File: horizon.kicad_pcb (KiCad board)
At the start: 4 copper layers, 50 x 100 mm, 261 parts, among them IC1 A3909, J1 Micro_SD_Card_Det1, J10 Conn_01x02_Pin, J11 USB_C_Receptacle_USB2.0_16P, J12 Conn_01x04, J13 1x3 servo, J14 1x3 servo, J15 arming terminal, J16 arming terminal, J17 arming terminal, J18 arming terminal, J19 Screw_Terminal_01x02, J2 Conn_02x03_Counter_Clockwise, J20 Screw_Terminal_01x02, J21 Screw_Terminal_01x02, J22 Screw_Terminal_01x02, J23 USB_C_Receptacle_USB2.0_16P, J24 USB_C_Receptacle_USB2.0_16P, J25 Conn_Coaxial, J3 Conn_Coaxial, J4 H9161TR-ND, J5 Screw_Term, J6 1x3 servo, J7 Conn_02x03_Counter_Clockwise, J8 Conn_02x03_Counter_Clockwise, J9 1x3 servo, Q1 IRLML6402, Q10 IRLML6402, Q11 IRLML6402, Q2 DMG2301L, Q3 IRLML6402, Q4 IRLML6402, Q5 IRLML6402, Q6 IRLML6402, Q7 BSS138, Q8 IRLML6402, Q9 IRLML6402, U1 MMCU, U10 LSM6DS3, U11 BGM220SC12WGA2R, U12 PE4259, U13 LTC4412xS6, U14 TPS61092, U15 AP2112K-3.3, U2 IMU, U3 NMCU, U4 TMCU, U5 LPS22HB, U6 GPS, U7 SX1276, U8 NAND, U9 TPS82130, Y1 Crystal, Y2 32.768kHz, Y4 32MHz

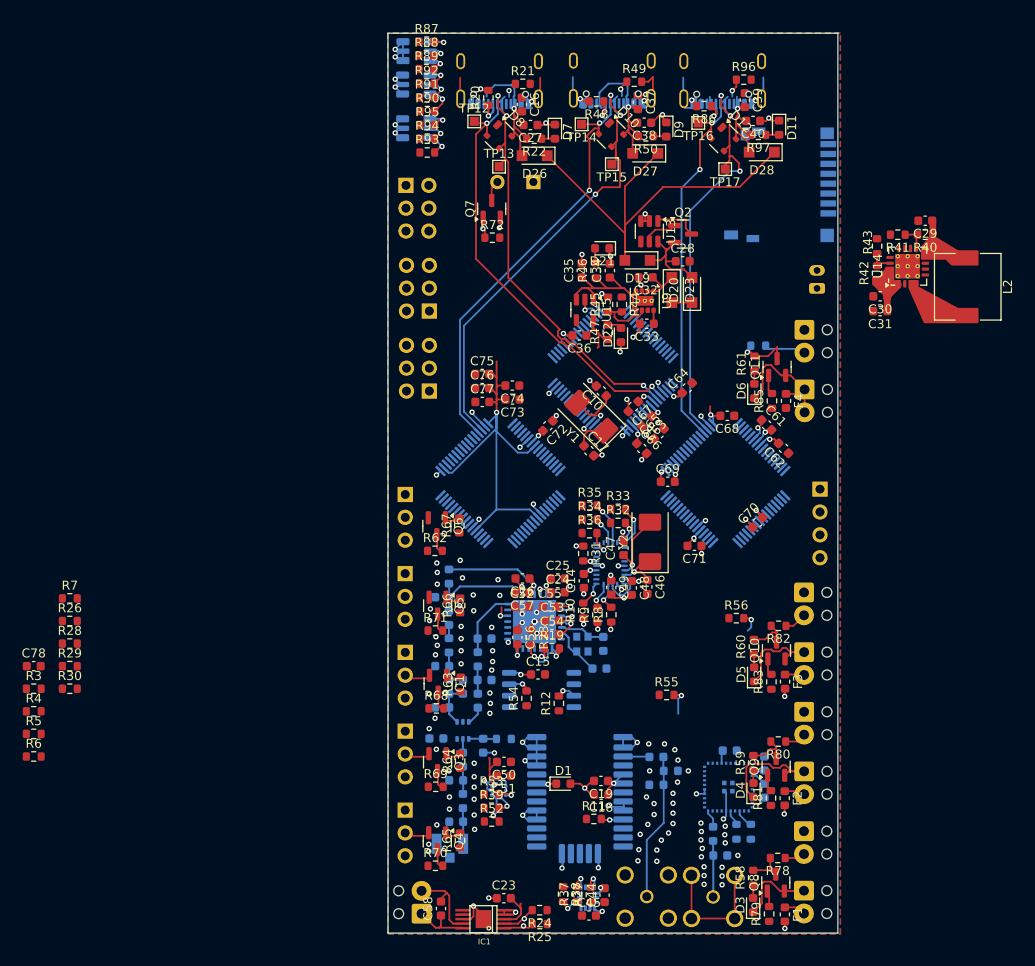
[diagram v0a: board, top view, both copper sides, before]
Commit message: flipped sides, changed footprint
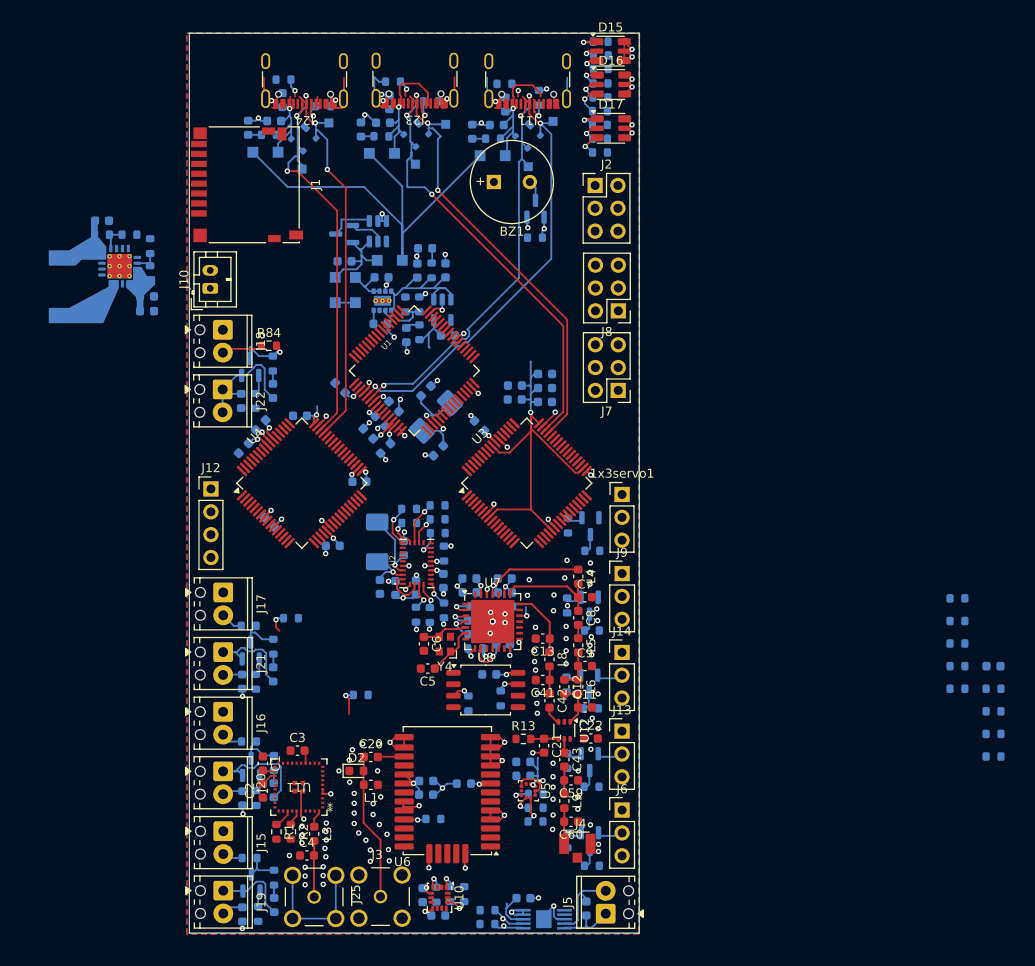
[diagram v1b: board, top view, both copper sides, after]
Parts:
- 1x3servo1: footprint Connector_PinSocket_2.54mm:PinSocket_1x03_P2.54mm_Vertical -> Connector_PinHeader_2.54mm:PinHeader_1x03_P2.54mm_Vertical; moved to F.Cu
- BZ1, C1, C11, C12, C13, C2, C20, C21, C22, C3, C4, C41, C42, C43, C5, C59, C6, C60, C7, C8, C9, D15, D16, D17, D2, J1, J10, J11, J13, J14, J15, J16, J17, J18, J19, J20, J21, J22, J23, J24, J25, J3, J4, J5, J6, J9, L1, L3, L4, L5, L6, L8, L9, R1, R13, R2, R84, U1, U10, U11, U12, U2, U3, U4, U5, U6, U7, U8, Y4: moved to F.Cu
- C10, C14, C15, C16, C17, C18, C19, C23, C24, C25, C26, C27, C28, C29, C30, C31, C32, C33, C34, C35, C36, C37, C38, C39, C40, C44, C45, C46, C47, C48, C49, C50, C51, C52, C53, C54, C55, C56, C57, C58, C61, C62, C63, C64, C65, C66, C67, C68, C69, C70, C71, C72, C73, C74, C75, C76, C77, C78, D1, D10, D11, D12, D19, D20, D21, D22, D23, D26, D27, D28, D3, D4, D5, D6, D7, D8, D9, F1, F2, F3, F4, IC1, L2, Q1, Q10, Q11, Q2, Q3, Q4, Q5, Q6, Q7, Q8, Q9, R10, R11, R12, R19, R20, R21, R22, R23, R24, R25, R26, R27, R28, R29, R3, R30, R31, R32, R33, R34, R35, R36, R37, R38, R39, R4, R40, R41, R42, R43, R44, R45, R46, R47, R48, R49, R5, R50, R52, R53, R54, R55, R56, R58, R59, R6, R60, R61, R62, R63, R64, R65, R66, R67, R68, R69, R7, R70, R71, R72, R78, R79, R8, R80, R81, R82, R83, R85, R86, R87, R88, R89, R9, R90, R91, R92, R93, R94, R95, R96, R97, TP12, TP13, TP14, TP15, TP16, TP17, U13, U14, U15, U9, Y1, Y2: moved to B.Cu
- J12: footprint Connector_PinSocket_2.54mm:PinSocket_1x04_P2.54mm_Vertical -> Connector_PinHeader_2.54mm:PinHeader_1x04_P2.54mm_Vertical; moved to F.Cu
- J2, J7, J8: footprint Connector_PinSocket_2.54mm:PinSocket_2x03_P2.54mm_Vertical -> Connector_PinHeader_2.54mm:PinHeader_2x03_P2.54mm_Vertical; moved to F.Cu
- moved C78 106.7 mm to (143.1, 86.4), turned to 180 degrees
- moved R3 106.7 mm to (143.1, 88.9), turned to 180 degrees
- moved R4 106.7 mm to (143.1, 91.4), turned to 180 degrees
- moved R5 106.7 mm to (143.1, 93.9), turned to 180 degrees
- moved R6 106.7 mm to (143.1, 96.5), turned to 180 degrees
- moved L2 100.9 mm to (39.3, 44.2)
- moved R26 98.6 mm to (139.1, 81.4), turned to 180 degrees
- moved R28 98.6 mm to (139.1, 83.9), turned to 180 degrees
- moved R29 98.6 mm to (139.1, 86.4), turned to 180 degrees
- moved R30 98.6 mm to (139.1, 88.9), turned to 180 degrees
- moved R7 98.6 mm to (139.1, 78.9), turned to 180 degrees
- moved C29 91.5 mm to (44.0, 36.9), turned to 0 degrees
- moved R40 91.5 mm to (44.0, 38.5), turned to 0 degrees
- moved U14 87.6 mm to (45.9, 42.0)
- moved R41 85.4 mm to (47.0, 38.5), turned to 0 degrees
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
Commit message: pcb
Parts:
- removed C78: 100nF, Capacitor_SMD:C_0603_1608Metric
- removed R26, R28, R29, R30: R, Resistor_SMD:R_0603_1608Metric
- removed R3, R4, R5: 10k, Resistor_SMD:R_0603_1608Metric
- removed R6, R7: 4.7k, Resistor_SMD:R_0603_1608Metric
- C30, C31, R42, R43, R56: moved to F.Cu
- moved R55 58.7 mm to (57.7, 32.9), turned to 0 degrees
- moved R56 53.1 mm to (68.8, 28.1)
- moved D16 43.2 mm to (57.5, 18.4), turned to 180 degrees
- moved D15 43.0 mm to (57.8, 23.3), turned to 180 degrees
- moved R87 42.8 mm to (57.5, 25.3), turned to 90 degrees
- moved R90 41.3 mm to (58.6, 17.8), turned to 0 degrees
- moved R88 41.3 mm to (58.4, 23.1), turned to 0 degrees
- moved R91 41.0 mm to (58.6, 19.3), turned to 0 degrees
- moved R92 40.9 mm to (58.5, 20.9), turned to 0 degrees
- moved R89 37.6 mm to (61.8, 21.1)
- moved L2 24.1 mm to (62.5, 37.7), turned to 0 degrees
- moved R40 19.0 mm to (60.0, 48.8), turned to -90 degrees
- moved C31 18.3 mm to (66.9, 43.5), turned to -90 degrees
- moved R41 17.9 mm to (61.6, 48.9), turned to 90 degrees
- moved C30 16.4 mm to (65.3, 43.5), turned to -90 degrees
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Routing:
- net 2G: track 0.00 -> 60.8 mm, vias 0 -> 1
- net 3B: track 0.00 -> 59.7 mm, vias 0 -> 1
- net 1G: track 0.00 -> 56.5 mm, vias 0 -> 3
- net 3G: track 0.00 -> 56.3 mm, vias 0 -> 1
- net Net-(L2-Pad2): track 0.00 -> 55.7 mm
- net 2R: track 0.00 -> 53.1 mm, vias 0 -> 3
- net +3.3V: track 117.3 -> 168.6 mm, vias 20 -> 24
- net 2B: track 0.00 -> 50.7 mm, vias 0 -> 1
- net 3R: track 0.00 -> 50.6 mm, vias 0 -> 1
- net 1R: track 0.00 -> 49.5 mm, vias 0 -> 1
- net NAND_MISO MMCU: track 0.00 -> 40.5 mm, vias 0 -> 2
- net 1B: track 0.00 -> 39.0 mm, vias 0 -> 3
- net Net-(J10-Pin_1): track 1.51 -> 37.0 mm
- net NAND_MOSI MMCU: track 0.00 -> 35.1 mm, vias 0 -> 2
- net bat: track 8.57 -> 32.7 mm, vias 0 -> 2
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
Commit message: kinda redid layout
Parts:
- removed J25, J3: Conn_Coaxial, Conn_Coaxial:LPRS_SMA_CONNECTOR
- removed J4: H9161TR-ND, H9161TR-ND:HRS_U.FL-R-SMT_01_
- removed U11: BGM220SC12WGA2R, BGM220SC12WGA2R:BGM220SC12WGA2R
- added C78: 100nF, Capacitor_SMD:C_0603_1608Metric, F.Cu at (73.0, 71.0)
- added R26: R, Resistor_SMD:R_0603_1608Metric, F.Cu at (56.5, 65.7)
- added R28: R, Resistor_SMD:R_0603_1608Metric, F.Cu at (70.6, 66.9)
- added R29: R, Resistor_SMD:R_0603_1608Metric, F.Cu at (73.1, 47.5)
- added R3: 10k, Resistor_SMD:R_0603_1608Metric, F.Cu at (96.2, 79.6)
- added R30: R, Resistor_SMD:R_0603_1608Metric, F.Cu at (75.8, 47.1)
- added R4: 10k, Resistor_SMD:R_0603_1608Metric, F.Cu at (67.5, 80.0)
- added R5: 10k, Resistor_SMD:R_0603_1608Metric, B.Cu at (60.5, 82.3)
- added R6: 4.7k, Resistor_SMD:R_0603_1608Metric, F.Cu at (84.0, 47.5)
- added R7: 4.7k, Resistor_SMD:R_0603_1608Metric, F.Cu at (85.1, 48.6)
- added REF**: MountingHole_2.1mm, MountingHole:MountingHole_2.1mm, F.Cu at (57.2, 19.9)
- added REF**: MountingHole_2.1mm, MountingHole:MountingHole_2.1mm, F.Cu at (99.3, 20.2)
- added REF**: MountingHole_2.1mm, MountingHole:MountingHole_2.1mm, F.Cu at (56.7, 113.0)
- 1x3servo1, BZ1, C11, C12, C13, C21, C22, C41, C42, C43, C59, C60, C7, C8, C9, J10, J11, J12, J13, J14, J15, J16, J17, J18, J19, J20, J21, J22, J23, J24, J5, J6, J9, L4, L5, L6, L8, L9, R13, U10, U12, U3, U4, U5, U6, U8: moved to B.Cu
- C10, C14, C15, C16, C17, C18, C19, C23, C24, C25, C26, C28, C29, C32, C33, C34, C35, C36, C37, C39, C44, C45, C46, C47, C48, C49, C50, C51, C52, C53, C54, C55, C56, C57, C58, C61, C62, C63, C64, C65, C66, C67, C68, C69, C70, C71, C72, C73, C74, C75, C76, C77, D1, D10, D11, D12, D19, D20, D21, D22, D23, D26, D27, D28, D3, D4, D5, D6, D7, D8, D9, F1, F2, F3, F4, IC1, L2, Q1, Q10, Q11, Q2, Q3, Q4, Q5, Q6, Q7, Q8, Q9, R10, R11, R19, R22, R23, R24, R25, R27, R31, R32, R33, R34, R35, R36, R37, R38, R39, R40, R41, R44, R45, R46, R47, R50, R52, R53, R55, R58, R59, R60, R61, R62, R63, R64, R65, R66, R67, R68, R69, R70, R71, R72, R78, R79, R8, R80, R81, R82, R83, R85, R87, R88, R89, R9, R90, R91, R92, R93, R94, R95, R97, TP12, TP13, TP14, TP15, TP16, TP17, U13, U14, U15, U9, Y1, Y2: moved to F.Cu
- U1: footprint MMCU:QFP50P1200X1200X160-64N -> MK20DX256VLH7:QFP50P1200X1200X160-64N; moved to B.Cu
- U2: footprint IMU:IC_BNO086 -> BNO086:IC_BNO086
- moved C4 254.4 mm to (-186.7, 129.6)
- moved C3 254.3 mm to (-186.7, 127.1)
- moved L3 250.0 mm to (-181.2, 129.3), turned to 0 degrees
- moved C1 249.8 mm to (-186.7, 122.0), turned to 0 degrees
- moved C2 249.7 mm to (-186.7, 124.5), turned to 0 degrees
- moved R2 247.7 mm to (-181.9, 125.1), turned to 0 degrees
- moved R1 245.9 mm to (-181.9, 122.6), turned to 0 degrees
- moved U2 169.2 mm to (-83.2, 123.2), turned to 0 degrees
- moved C49 146.4 mm to (-53.6, 139.9), turned to 0 degrees
- moved Y2 145.8 mm to (-51.6, 145.5), turned to 0 degrees
- moved C14 145.8 mm to (-49.7, 139.6)
- moved C47 144.9 mm to (-53.6, 134.9), turned to 0 degrees
- moved R35 143.4 mm to (-41.6, 142.4), turned to 0 degrees
- moved C48 143.2 mm to (-53.6, 137.4), turned to 0 degrees
- moved R36 143.1 mm to (-41.6, 144.9), turned to 0 degrees
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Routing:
- net GND: track 201.1 -> 1.90 mm, vias 161 -> 0
- net +3.3V: track 168.6 -> 14.8 mm, vias 24 -> 0
- net 2G: track 60.8 -> 0.00 mm, vias 1 -> 0
- net 3B: track 59.7 -> 0.00 mm, vias 1 -> 0
- net 1G: track 56.5 -> 0.00 mm, vias 3 -> 0
- net 3G: track 56.3 -> 0.00 mm, vias 1 -> 0
- net VBUS: track 53.5 -> 0.00 mm
- net 2R: track 53.1 -> 0.00 mm, vias 3 -> 0
- net D- DMCU-1: track 50.8 -> 0.00 mm, vias 3 -> 0
- net 2B: track 50.7 -> 0.00 mm, vias 1 -> 0
- net 3R: track 50.6 -> 0.00 mm, vias 1 -> 0
- net 1R: track 49.5 -> 0.00 mm, vias 1 -> 0
- net D+ MMCU: track 49.5 -> 0.00 mm, vias 2 -> 0
- net D+ DMCU-1: track 48.9 -> 0.00 mm, vias 2 -> 0
- net D- MMCU: track 46.9 -> 0.00 mm, vias 3 -> 0
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- removed copper zone on B.Cu, net GND
- removed copper zone on F.Cu, net GND

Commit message: finished layout
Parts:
- added J25: Conn_Coaxial, SMA_CONNECTOR:LPRS_SMA_CONNECTOR, B.Cu at (81.8, 34.7)
- added J3: Conn_Coaxial, SMA_CONNECTOR:LPRS_SMA_CONNECTOR, B.Cu at (89.1, 34.7)
- added U11: BGM220SC12WGA2R, KiCADv6:BGM220SC12WGA2R, B.Cu at (82.1, 42.7)
- U2: moved to B.Cu
- moved C4 282.3 mm to (79.4, 35.2)
- moved C3 281.9 mm to (82.8, 44.4), turned to -90 degrees
- moved R1 278.8 mm to (84.0, 38.7)
- moved L3 278.5 mm to (81.8, 37.7), turned to 90 degrees
- moved C2 278.4 mm to (79.3, 42.3), turned to -90 degrees
- moved C1 275.9 mm to (77.8, 43.3), turned to -90 degrees
- moved R2 275.9 mm to (80.9, 40.9), turned to -90 degrees
- moved U2 162.8 mm to (74.6, 83.4), turned to -90 degrees
- moved C49 141.9 mm to (76.0, 82.3), turned to 180 degrees
- moved C14 140.9 mm to (79.0, 82.3), turned to 180 degrees
- moved C48 140.3 mm to (76.0, 83.8), turned to 180 degrees
- moved R10 138.2 mm to (77.7, 80.0), turned to -90 degrees
- moved Y2 137.8 mm to (70.3, 81.4), turned to -90 degrees
- moved C46 137.5 mm to (73.1, 79.0), turned to 90 degrees
- moved C47 136.5 mm to (73.3, 84.6), turned to -90 degrees
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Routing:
- net +3.3V: track 14.8 -> 16.7 mm
